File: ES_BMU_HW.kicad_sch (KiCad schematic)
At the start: 0 parts

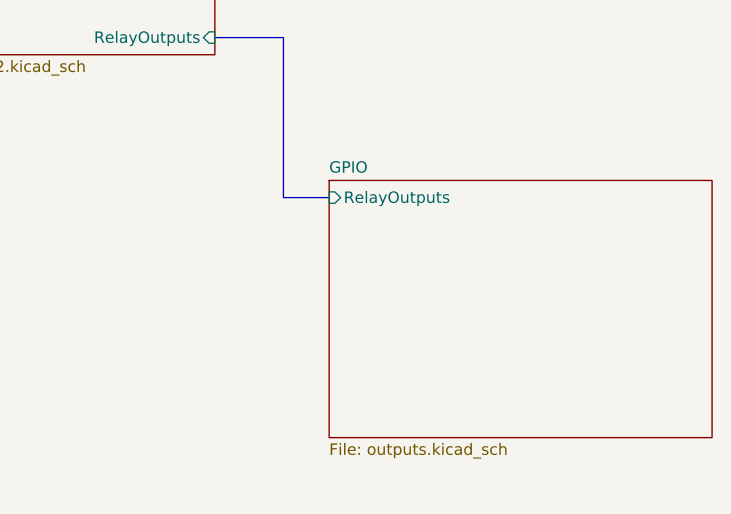
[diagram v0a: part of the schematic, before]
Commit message: correció dels outputs al GPIO
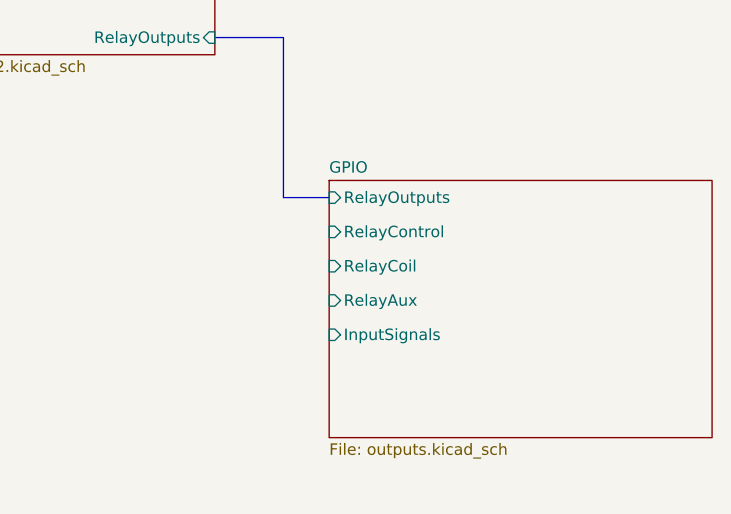
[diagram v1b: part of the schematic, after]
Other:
- sheet GPIO ports: added InputSignals, RelayAux, RelayCoil, RelayControl; removed none
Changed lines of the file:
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@@
 			)
 		)
-		(instances
-			(project "BMSems"
+		(pin "RelayControl" input
+			(at 187.96 128.27 180)
+			(effects
+				(font
+					(size 1.27 1.27)
+				)
+				(justify left)
+			)
+		)
+		(pin "RelayCoil" input
+			(at 187.96 132.08 180)
+			(effects
+				(font
+					(size 1.27 1.27)
+				)
+				(justify left)
+			)
+		)
+		(pin "RelayAux" input
+			(at 187.96 135.89 180)
+			(effects
+				(font
+					(size 1.27 1.27)
+				)
+				(justify left)
+			)
+		)
+		(pin "InputSignals" input
+			(at 187.96 139.7 180)
+			(effects
+				(font
+					(size 1.27 1.27)
+				)
+				(justify left)
+			)
+		)
+		(instances
+			(project "ES_BMU_HW"
 				(path "/241310d7-2595-46fd-a468-4bac14ba2b52"
 					(page "5")
@@
 		)
 		(instances
-			(project "BMSems"
+			(project "ES_BMU_HW"
 				(path "/241310d7-2595-46fd-a468-4bac14ba2b52"
 					(page "3")
@@
 		)
 		(instances
-			(project "BMSems"
+			(project "ES_BMU_HW"
 				(path "/241310d7-2595-46fd-a468-4bac14ba2b52"
 					(page "4")
@@
 		)
 		(instances
-			(project "BMSems"
+			(project "ES_BMU_HW"
 				(path "/241310d7-2595-46fd-a468-4bac14ba2b52"
 					(page "2")
@@
 		)
 		(instances
-			(project "BMSems"
+			(project "ES_BMU_HW"
 				(path "/241310d7-2595-46fd-a468-4bac14ba2b52"
 					(page "6")

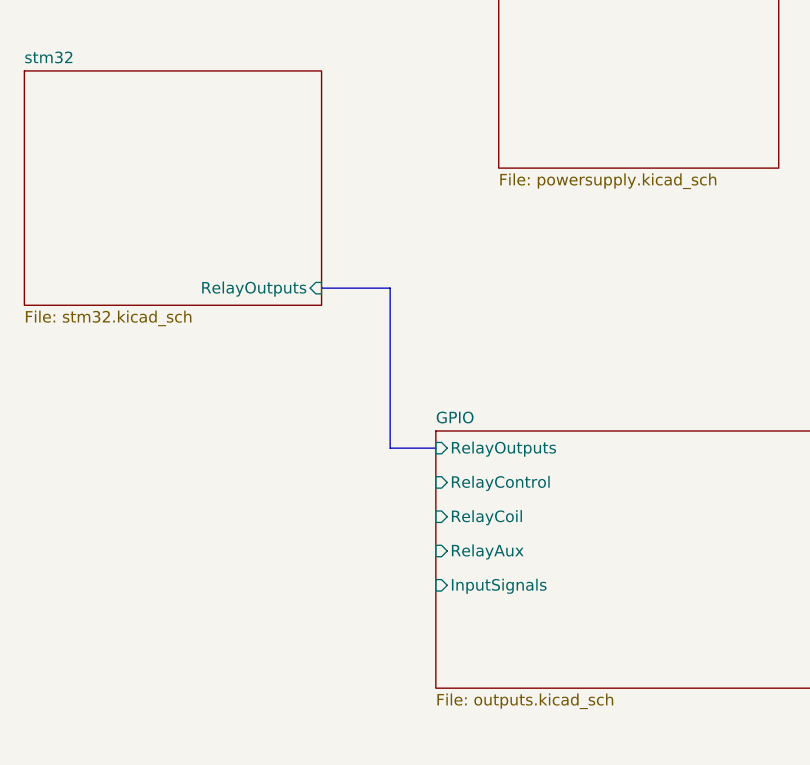
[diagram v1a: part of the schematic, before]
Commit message: Canvi de microcontrolador Control dels relés de potència actualitzat Leds afegits per a visualitzar l'estat del fusible
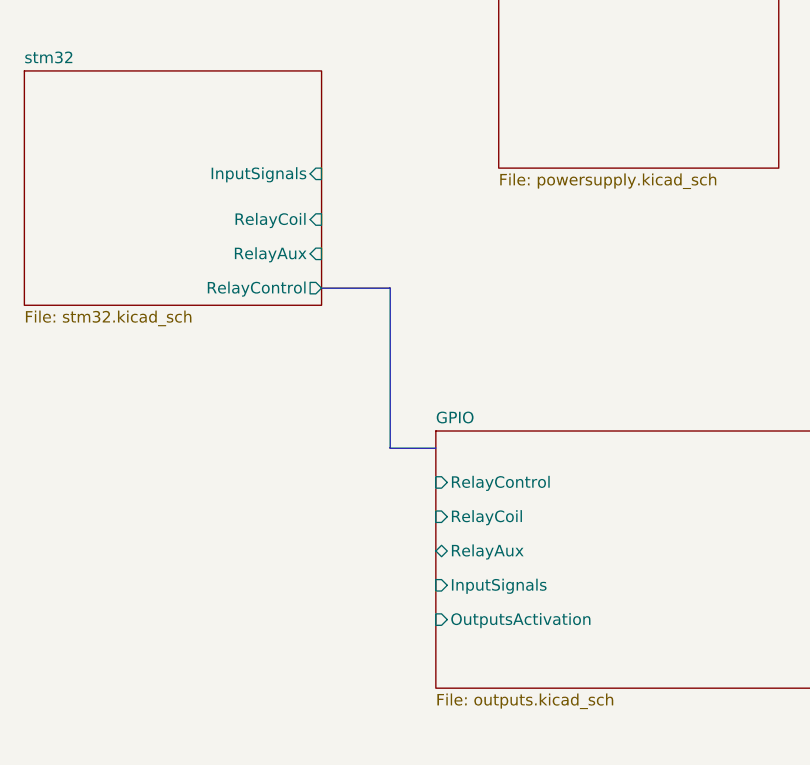
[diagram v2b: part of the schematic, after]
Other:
- sheet GPIO ports: added OutputsActivation; removed RelayOutputs
- sheet stm32 ports: added InputSignals, RelayAux, RelayCoil, RelayControl; removed RelayOutputs
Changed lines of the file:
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@@
-			)
-		)
-		(pin "RelayOutputs" input
-			(at 187.96 124.46 180)
-			(effects
-				(font
-					(size 1.27 1.27)
-				)
-				(justify left)
 			)
 		)
@@
 			)
 		)
-		(pin "RelayAux" input
+		(pin "RelayAux" bidirectional
 			(at 187.96 135.89 180)
 			(effects
@@
 		(pin "InputSignals" input
 			(at 187.96 139.7 180)
+			(effects
+				(font
+					(size 1.27 1.27)
+				)
+				(justify left)
+			)
+		)
+		(pin "OutputsActivation" input
+			(at 187.96 143.51 180)
 			(effects
 				(font
@@
 			)
 		)
-		(pin "RelayOutputs" input
+		(pin "RelayControl" output
 			(at 175.26 106.68 0)
 			(effects
 				(font
+					(size 1.27 1.27)
+				)
+				(justify right)
+			)
+		)
+		(pin "RelayCoil" input
+			(at 175.26 99.06 0)
+			(effects
+				(font
+					(size 1.27 1.27)
+				)
+				(justify right)
+			)
+		)
+		(pin "RelayAux" input
+			(at 175.26 102.87 0)
+			(effects
+				(font
+					(size 1.27 1.27)
+				)
+				(justify right)
+			)
+		)
+		(pin "InputSignals" input
+			(at 175.26 93.98 0)
+			(effects
+				(font

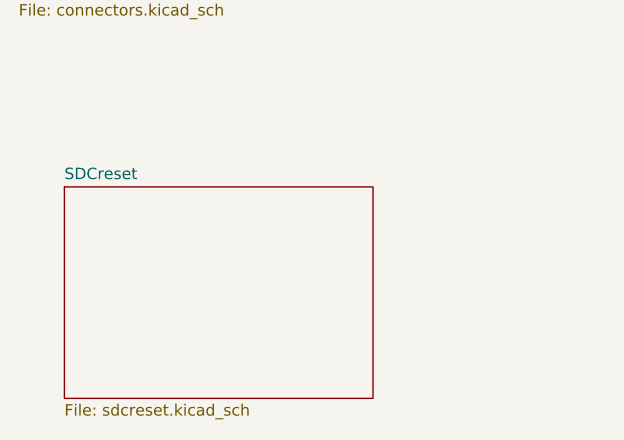
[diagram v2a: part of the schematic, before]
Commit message: - Reorganització dels components al fitxer de stm32 - S'ha afegit el ADC ADS1113IDGS per la lectura del sensor Hall - Modificació del tranceptor CAN al SN65HVD234 - Eliminació del pin SWO - S'ha afegit el pin de enable per a cada tranceptor
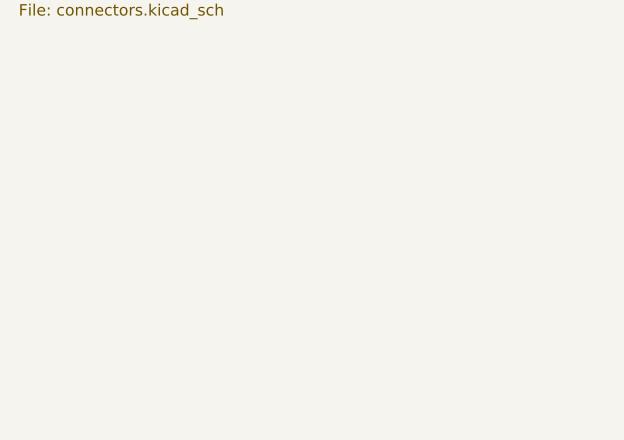
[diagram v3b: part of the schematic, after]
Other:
- removed sheet SDCreset
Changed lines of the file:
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@@
-		)
-	)
-	(sheet
-		(at 88.9 131.445)
-		(size 34.29 23.495)
-		(exclude_from_sim no)
-		(in_bom yes)
-		(on_board yes)
-		(dnp no)
-		(fields_autoplaced yes)
-		(stroke
-			(width 0.1524)
-			(type solid)
-		)
-		(fill
-			(color 0 0 0 0.0000)
-		)
-		(property "Sheetname" "SDCreset"
-			(at 88.9 130.7334 0)
-			(effects
-				(font
-					(size 1.27 1.27)
-				)
-				(justify left bottom)
-			)
-		)
-		(property "Sheetfile" "sdcreset.kicad_sch"
-			(at 88.9 155.5246 0)
-			(effects
-				(font
-					(size 1.27 1.27)
-				)
-				(justify left top)
-			)
-		)
-		(instances
-			(project "ES_BMU_HW"
-				(path "/241310d7-2595-46fd-a468-4bac14ba2b52"
-					(page "6")
-				)
-			)
 		)
 	)

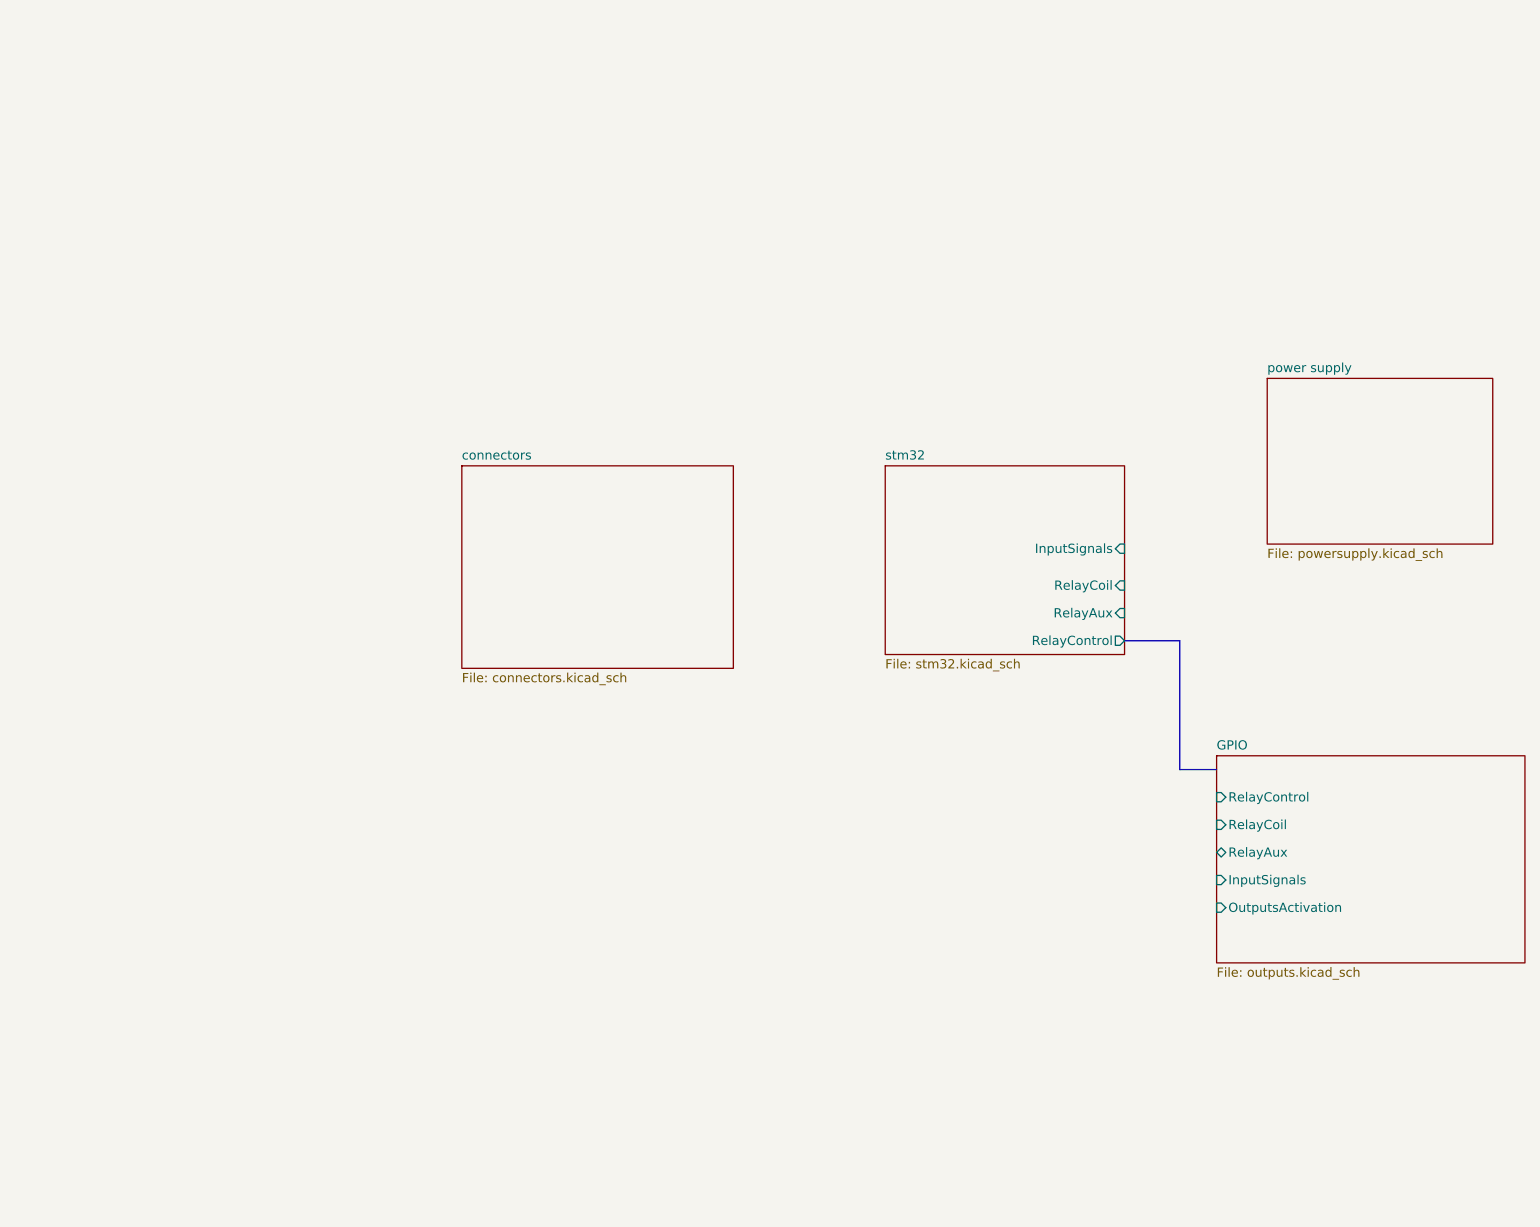
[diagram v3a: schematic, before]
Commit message: Modificació de les etiquetes a globals Filtre afegit al transformador de isoSPI Leds indicadors per estat i error Senyal d'error de BMS per el sdcreset
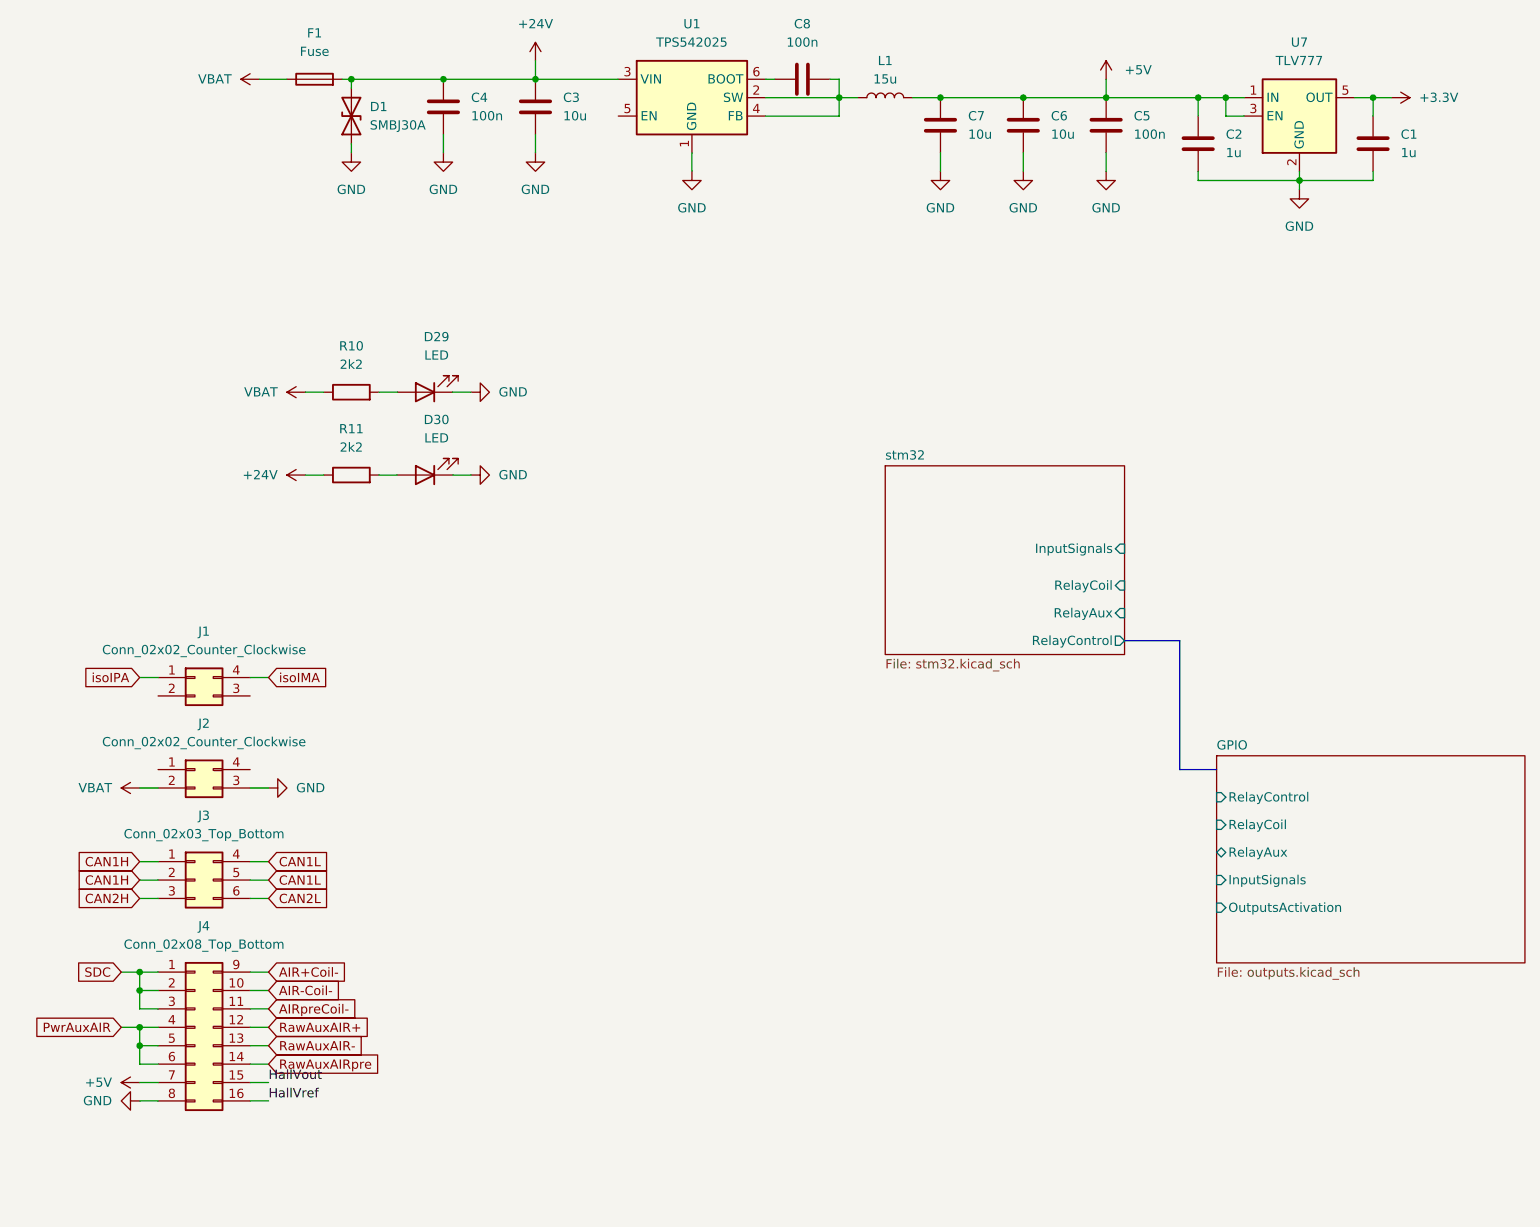
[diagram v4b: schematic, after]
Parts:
- added C1, C2: 1u, Capacitor_SMD:C_0603_1608Metric_Pad1.08x0.95mm_HandSolder, symbol Device:C
- added C3, C6, C7: 10u, Capacitor_SMD:C_0603_1608Metric_Pad1.08x0.95mm_HandSolder, symbol Device:C
- added C4, C5, C8: 100n, Capacitor_SMD:C_0603_1608Metric_Pad1.08x0.95mm_HandSolder, symbol Device:C
- added D1: SMBJ30A, Diode_SMD:D_SMB, symbol Device:D_TVS
- added D29, D30: LED, symbol Device:LED
- added F1: Fuse, Fuse:Fuse_1206_3216Metric_Pad1.42x1.75mm_HandSolder, symbol Device:Fuse
- added J1, J2: Conn_02x02_Counter_Clockwise, Connector_Molex:Molex_Nano-Fit_105314-xx04_2x02_P2.50mm_Horizontal, symbol Connector_Generic:Conn_02x02_Counter_Clockwise
- added J3: Conn_02x03_Top_Bottom, Connector_Molex:Molex_Nano-Fit_105314-xx06_2x03_P2.50mm_Horizontal, symbol Connector_Generic:Conn_02x03_Top_Bottom
- added J4: Conn_02x08_Top_Bottom, Connector_Molex:Molex_Nano-Fit_105314-xx16_2x08_P2.50mm_Horizontal, symbol Connector_Generic:Conn_02x08_Top_Bottom
- added L1: 15u, symbol Device:L
- added R10, R11: 2k2, Resistor_SMD:R_0201_0603Metric_Pad0.64x0.40mm_HandSolder, symbol Device:R
- added U1: TPS542025, Package_TO_SOT_SMD:SOT-23-6, symbol Regulator_Switching:TPS54202DDC
- added U7: TLV777, Package_TO_SOT_SMD:SOT-23-5, symbol Regulator_Linear:TPS77012PDBV
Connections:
- new net: D29.2 (A), R10.2
- new net: C8.1, U1.6 (BOOT)
- new net: C8.2, L1.1, U1.2 (SW), U1.4 (FB)
- new net: D30.2 (A), R11.2
- new net +24V: C3.1, C4.1, D1.2 (A2), F1.2, R11.1, U1.3 (VIN)
- new net +3.3V: C1.1, U7.5 (OUT)
- new net +5V: C2.1, C5.1, C6.1, C7.1, J4.7 (Pin_7), L1.2, U7.1 (IN), U7.3 (EN)
- new net AIR+Coil-: J4.9 (Pin_9)
- new net AIR-Coil-: J4.10 (Pin_10)
- new net AIRpreCoil-: J4.11 (Pin_11)
- new net CAN1H: J3.1 (Pin_1), J3.2 (Pin_2)
- new net CAN1L: J3.4 (Pin_4), J3.5 (Pin_5)
- new net CAN2H: J3.3 (Pin_3)
- new net CAN2L: J3.6 (Pin_6)
- new net GND: C1.2, C2.2, C3.2, C4.2, C5.2, C6.2, C7.2, D1.1 (A1), D29.1 (K), D30.1 (K), J2.3 (Pin_3), J4.8 (Pin_8), U1.1 (GND), U7.2 (GND), U7.4 (GND)
- new net HallVout: J4.15 (Pin_15)
- new net HallVref: J4.16 (Pin_16)
- new net PwrAuxAIR: J4.4 (Pin_4), J4.5 (Pin_5), J4.6 (Pin_6)
- new net RawAuxAIR+: J4.12 (Pin_12)
- new net RawAuxAIR-: J4.13 (Pin_13)
- new net RawAuxAIRpre: J4.14 (Pin_14)
- new net SDC: J4.1 (Pin_1), J4.2 (Pin_2), J4.3 (Pin_3)
- new net VBAT: F1.1, J2.2 (Pin_2), R10.1
- new net isoIMA: J1.4 (Pin_4)
- new net isoIPA: J1.1 (Pin_1)
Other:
- removed sheet connectors
- removed sheet power supply

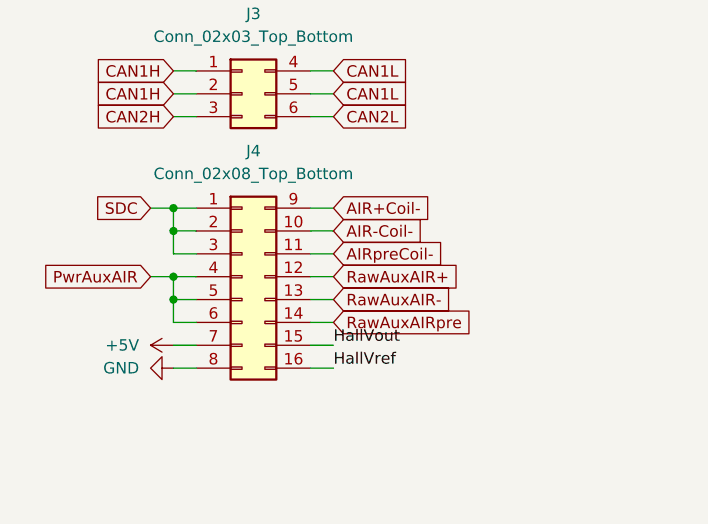
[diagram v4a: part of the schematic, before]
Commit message: Revisió dels valors de filtres, divisors de tensió i resistències
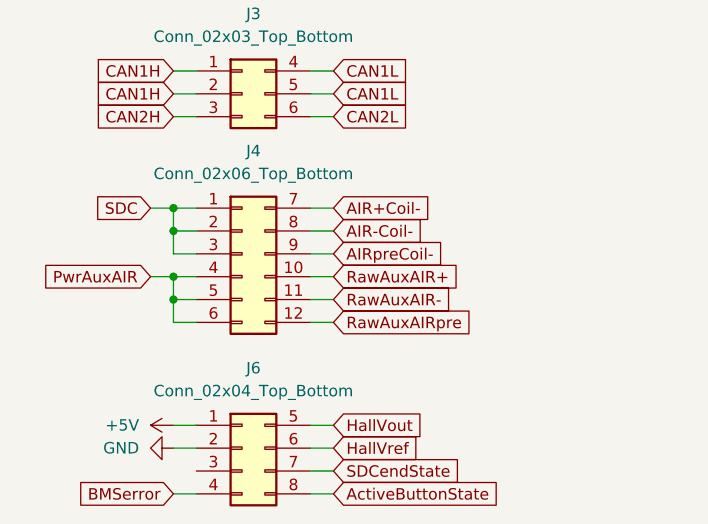
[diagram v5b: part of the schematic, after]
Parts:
- removed J4: Conn_02x08_Top_Bottom, Connector_Molex:Molex_Nano-Fit_105314-xx16_2x08_P2.50mm_Horizontal, symbol Connector_Generic:Conn_02x08_Top_Bottom
- added J4: Conn_02x06_Top_Bottom, Connector_Molex:Molex_Nano-Fit_105314-xx12_2x06_P2.50mm_Horizontal, symbol Connector_Generic:Conn_02x06_Top_Bottom
- added J6: Conn_02x04_Top_Bottom, Connector_Molex:Molex_Nano-Fit_105314-xx08_2x04_P2.50mm_Horizontal, symbol Connector_Generic:Conn_02x04_Top_Bottom
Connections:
- net +5V: now also J6.1 (Pin_1)
- net AIR+Coil-: now also J4.7 (Pin_7)
- net AIR-Coil-: now also J4.8 (Pin_8)
- net AIRpreCoil-: now also J4.9 (Pin_9)
- net GND: now also J6.2 (Pin_2)
- net HallVout: now also J6.5 (Pin_5)
- net HallVref: now also J6.6 (Pin_6)
- net PwrAuxAIR: now also J4.4 (Pin_4), J4.5 (Pin_5), J4.6 (Pin_6)
- net RawAuxAIR+: now also J4.10 (Pin_10)
- net RawAuxAIR-: now also J4.11 (Pin_11)
- net RawAuxAIRpre: now also J4.12 (Pin_12)
- net SDC: now also J4.1 (Pin_1), J4.2 (Pin_2), J4.3 (Pin_3)
- new net ActiveButtonState: J6.8 (Pin_8)
- new net BMSerror: J6.4 (Pin_4)
- new net SDCendState: J6.7 (Pin_7)
